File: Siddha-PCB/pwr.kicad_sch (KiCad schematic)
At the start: 3 parts

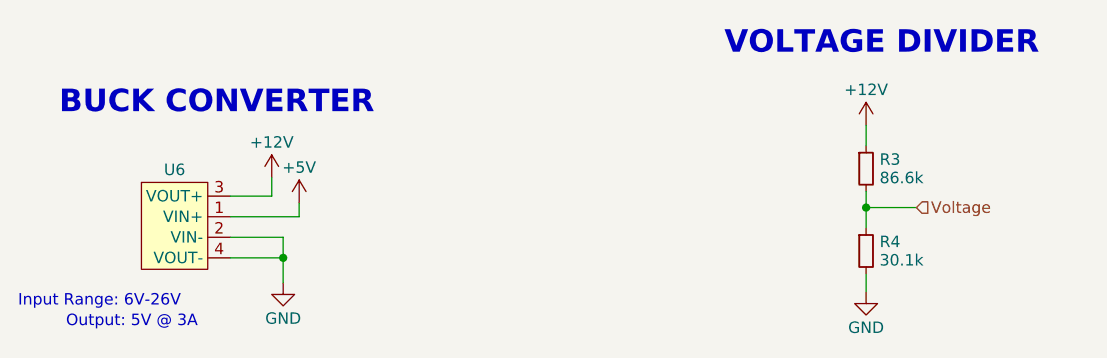
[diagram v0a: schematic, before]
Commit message: switch to linear actuator and 7.4v battery
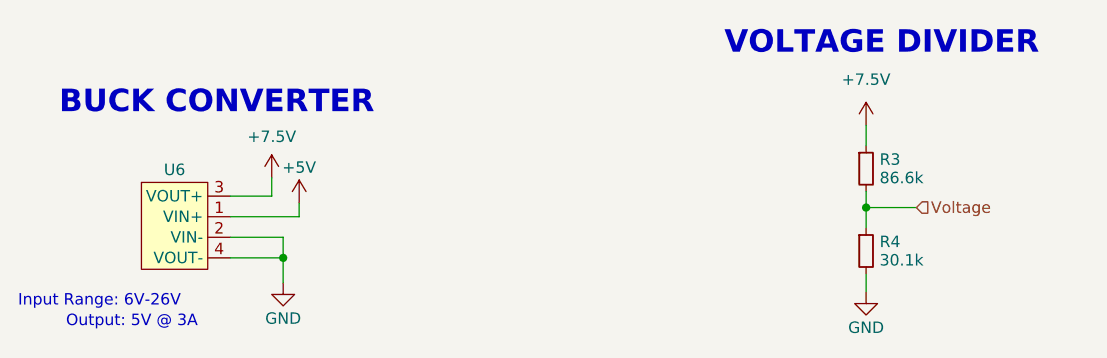
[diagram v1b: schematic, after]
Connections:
- net +12V renamed +7.5V
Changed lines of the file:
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@@
     )
   )
-  (symbol (lib_id "power:+12V") (at 213.106 87.63 0) (unit 1)
+  (symbol (lib_id "power:+7.5V") (at 147.066 93.472 0) (unit 1)
     (in_bom yes) (on_board yes) (dnp no) (fields_autoplaced)
-    (property "Reference" "#PWR028" (at 213.106 91.44 0)
+    (property "Reference" "#PWR021" (at 147.066 97.282 0)
       (effects (font (size 1.27 1.27)) hide)
     )
-    (property "Value" "+12V" (at 213.106 83.685 0)
+    (property "Value" "+7.5V" (at 147.066 88.9 0)
       (effects (font (size 1.27 1.27)))
     )
-    (property "Footprint" "" (at 213.106 87.63 0)
+    (property "Footprint" "" (at 147.066 93.472 0)
       (effects (font (size 1.27 1.27)) hide)
     )
-    (property "Datasheet" "" (at 213.106 87.63 0)
+    (property "Datasheet" "" (at 147.066 93.472 0)
       (effects (font (size 1.27 1.27)) hide)
     )
@@
       (project "RocketryIN-FC"
         (path "/eca5bcb3-e8cc-4774-b734-f4245bf2d59b/5057bef7-2079-475f-a386-12f7b9f3109d"
-          (reference "#PWR028") (unit 1)
+          (reference "#PWR021") (unit 1)
         )
       )
@@
     )
   )
-  (symbol (lib_id "power:+12V") (at 147.066 93.472 0) (unit 1)
+  (symbol (lib_id "power:+7.5V") (at 213.106 87.63 0) (unit 1)
     (in_bom yes) (on_board yes) (dnp no) (fields_autoplaced)
-    (property "Reference" "#PWR026" (at 147.066 97.282 0)
+    (property "Reference" "#PWR022" (at 213.106 91.44 0)
       (effects (font (size 1.27 1.27)) hide)
     )
-    (property "Value" "+12V" (at 147.066 89.527 0)
+    (property "Value" "+7.5V" (at 213.106 82.55 0)
       (effects (font (size 1.27 1.27)))
     )
-    (property "Footprint" "" (at 147.066 93.472 0)
+    (property "Footprint" "" (at 213.106 87.63 0)
       (effects (font (size 1.27 1.27)) hide)
     )
-    (property "Datasheet" "" (at 147.066 93.472 0)
+    (property "Datasheet" "" (at 213.106 87.63 0)
       (effects (font (size 1.27 1.27)) hide)
     )
@@
       (project "RocketryIN-FC"
         (path "/eca5bcb3-e8cc-4774-b734-f4245bf2d59b/5057bef7-2079-475f-a386-12f7b9f3109d"
-          (reference "#PWR026") (unit 1)
+          (reference "#PWR022") (unit 1)
         )
       )
